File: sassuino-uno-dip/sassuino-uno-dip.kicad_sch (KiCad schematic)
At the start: 33 parts, among them J1 USB_B, J10 OSCPWR_HDR, J2 POWER2_HDR, J3 ICSP_HDR, J4 POWER_HDR, J5 PORTC_HDR, J6 PORTB_HDR, J7 PORTD_HDR, J8 XTAL2_HDR, J9 XTAL1_HDR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

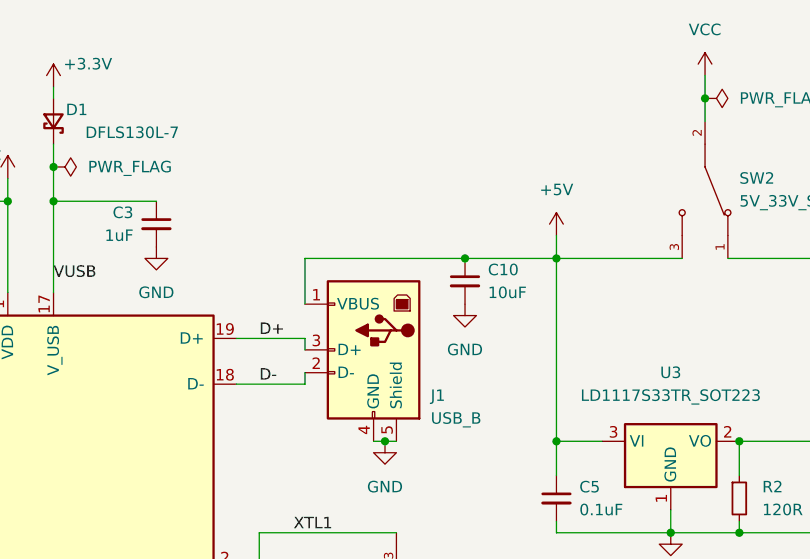
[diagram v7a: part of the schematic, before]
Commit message: Add a polyfuse on VBUS.
Also ditch the VBUS decoupling cap, I don't recall why I added it.
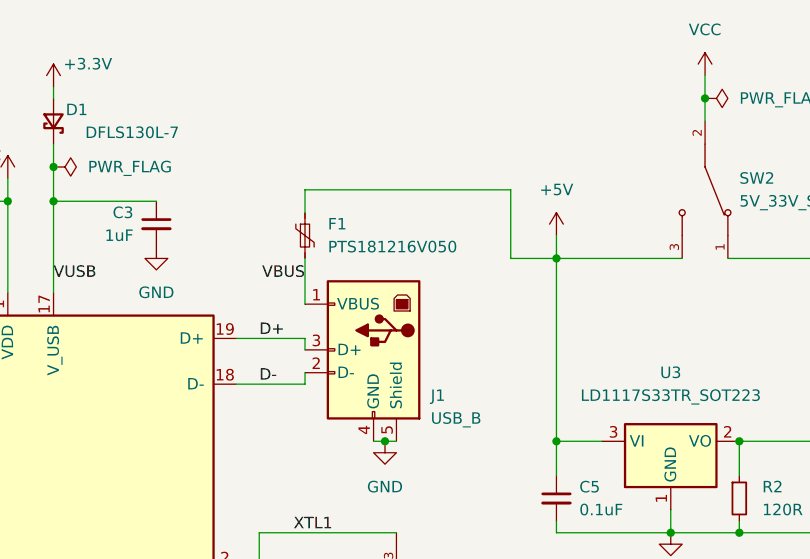
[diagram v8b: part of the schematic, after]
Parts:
- removed C10: 10uF, Capacitor_SMD:C_1206_3216Metric, symbol Device:C_Small
- added F1: PTS181216V050, Fuse:Fuse_1812_4532Metric, symbol Device:Polyfuse_Small
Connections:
- net +5V: now also F1.1; no longer J1.1 (VBUS)
- new net VBUS: F1.2, J1.1 (VBUS)
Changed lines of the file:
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@@
-		(color 0 0 0 0)
-	)
-	(junction
-		(at 218.44 44.45)
-		(diameter 0)
 		(color 0 0 0 0)
 	)
@@
 	(wire
 		(pts
+			(xy 200.66 39.37) (xy 200.66 36.83)
+		)
+		(stroke
+			(width 0)
+			(type default)
+		)
+	)
+	(wire
+		(pts
 			(xy 135.89 123.19) (xy 138.43 123.19)
 		)
@@
 	(wire
 		(pts
-			(xy 200.66 44.45) (xy 218.44 44.45)
-		)
-		(stroke
-			(width 0)
-			(type default)
-		)
-	)
-	(wire
-		(pts
 			(xy 27.94 35.56) (xy 31.75 35.56)
 		)
@@
 	(wire
 		(pts
-			(xy 218.44 44.45) (xy 228.6 44.45)
-		)
-		(stroke
-			(width 0)
-			(type default)
-		)
-	)
-	(wire
-		(pts
 			(xy 146.05 58.42) (xy 147.32 58.42)
 		)
@@
 	(wire
 		(pts
+			(xy 223.52 44.45) (xy 228.6 44.45)
+		)
+		(stroke
+			(width 0)
+			(type default)
+		)
+	)
+	(wire
+		(pts
 			(xy 172.72 34.29) (xy 172.72 38.1)
 		)
@@
 	(wire
 		(pts
+			(xy 200.66 36.83) (xy 223.52 36.83)
+		)
+		(stroke
+			(width 0)
+			(type default)
+		)
+	)
+	(wire
+		(pts
 			(xy 58.42 53.34) (xy 60.96 53.34)
 		)
@@
 		(pts
 			(xy 132.08 185.42) (xy 138.43 185.42)
+		)
+		(stroke
+			(width 0)
+			(type default)
+		)
+	)
+	(wire
+		(pts
+			(xy 223.52 36.83) (xy 223.52 44.45)
 		)
 		(stroke
@@
 		)
 	)
+	(label "VBUS"
+		(at 200.66 46.99 180)
+		(effects
+			(font
+				(size 1.27 1.27)
+			)
+			(justify right bottom)
+		)
+	)
 	(label "PD7"
 		(at 132.08 170.18 180)
@@
 	)
 	(symbol
-		(lib_id "power:GND")
-		(at 218.44 49.53 0)
+		(lib_id "Device:Polyfuse_Small")
+		(at 200.66 41.91 0)
 		(unit 1)
 		(exclude_from_sim no)
@@
 		(on_board yes)
 		(dnp no)
-		(fields_autoplaced yes)
-		(property "Reference" "#PWR04"
-			(at 218.44 55.88 0)
-			(effects
-				(font
-					(size 1.27 1.27)
-				)
-				(hide yes)
-			)
-		)
-		(property "Value" "GND"
-			(at 218.44 54.61 0)
-			(effects
-				(font
-					(size 1.27 1.27)
-				)
-			)
-		)
-		(property "Footprint" ""
-			(at 218.44 49.53 0)
-			(effects
-				(font
-					(size 1.27 1.27)
-				)
-				(hide yes)
-			)
-		)
-		(property "Datasheet" ""
-			(at 218.44 49.53 0)
-			(effects
-				(font
-					(size 1.27 1.27)
-				)
-				(hide yes)
-			)
-		)
-		(property "Description" "Power symbol creates a global label with name \"GND\" , ground"
-			(at 218.44 49.53 0)
-			(effects
-				(font
-					(size 1.27 1.27)
-				)
-				(hide yes)
-			)
+		(property "Reference" "F1"
+			(at 203.2 40.6399 0)
+			(effects
+				(font
+					(size 1.27 1.27)
+				)
+				(justify left)
+			)
+		)
+		(property "Value" "PTS181216V050"
+			(at 203.2 43.1799 0)
+			(effects
+				(font
+					(size 1.27 1.27)
+				)
+				(justify left)
+			)
+		)
+		(property "Footprint" "Fuse:Fuse_1812_4532Metric"
+			(at 201.93 46.99 0)
+			(effects
+				(font
+					(size 1.27 1.27)
+				)
+				(justify left)
+				(hide yes)
+			)
+		)
+		(property "Datasheet" "~"
+			(at 200.66 41.91 0)
+			(effects
+				(font
+					(size 1.27 1.27)
+				)
+				(hide yes)
+			)
+		)
+		(property "Description" "Resettable fuse, polymeric positive temperature coefficient, small symbol"
+			(at 200.66 41.91 0)
+			(effects
+				(font
+					(size 1.27 1.27)
+				)
+				(hide yes)
+			)
+		)
+		(pin "2"
 		)
 		(pin "1"
@@
 			(project ""
 				(path "/93924f32-2dd0-417f-984a-e4a0b078075b"
-					(reference "#PWR04")
+					(reference "F1")
 					(unit 1)
 				)
@@
 					(unit 1)
 				)
-			)
-		)
-	)
-	(symbol
-		(lib_id "Device:C_Small")
-		(at 218.44 46.99 0)
-		(unit 1)
-		(exclude_from_sim no)
-		(in_bom yes)
-		(on_board yes)
-		(dnp no)
-		(fields_autoplaced yes)
-		(property "Reference" "C10"
-			(at 220.98 45.7262 0)
-			(effects
-				(font
-					(size 1.27 1.27)
-				)
-				(justify left)
-			)
-		)
-		(property "Value" "10uF"
-			(at 220.98 48.2662 0)
-			(effects
-				(font
-					(size 1.27 1.27)
-				)
-				(justify left)
-			)
-		)
-		(property "Footprint" "Capacitor_SMD:C_1206_3216Metric"
-			(at 218.44 46.99 0)
-			(effects
-				(font
-					(size 1.27 1.27)
-				)
-				(hide yes)
-			)
-		)
-		(property "Datasheet" "~"
-			(at 218.44 46.99 0)
-			(effects
-				(font
-					(size 1.27 1.27)
-				)
-				(hide yes)
-			)
-		)
-		(property "Description" "Unpolarized capacitor, small symbol"
-			(at 218.44 46.99 0)
-			(effects
-				(font
-					(size 1.27 1.27)
-				)
-				(hide yes)
-			)
-		)
-		(pin "1"
-		)
-		(pin "2"
-		)
-		(instances
-			(project ""
-				(path "/93924f32-2dd0-417f-984a-e4a0b078075b"
-					(reference "C10")
-					(unit 1)
-				)
